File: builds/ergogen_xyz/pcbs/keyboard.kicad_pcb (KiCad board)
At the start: 2 copper layers, 248 x 123.7 mm, 72 parts

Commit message: Phase 2: assembly hardware, wood cutting files, combined 3D render
- Add M2 mounting holes to PCB and outlines (4 corners per half)
- Add frame_with_holes outline for wood CNC/laser cutting
- Generate assembly.scad stacking all layers (frame, plates, PCB)
- Render assembly.png via OpenSCAD
- Update BOM with Phase 1 tenting mount and Phase 2 screws/standoffs
- Update render.md with assembly and wood cutting viewing instructions
- Update generate.sh with assembly generation and OpenSCAD render step

Co-Authored-By: Claude Opus 4.6 <noreply@anthropic.com>
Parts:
- added MH1: , MountingHole_M2, F.Cu at (0.28, -43.3)
- added MH2: , MountingHole_M2, F.Cu at (-5.57, 4.35)
- added MH3: , MountingHole_M2, F.Cu at (90.5, -33.5)
- added MH4: , MountingHole_M2, F.Cu at (80.6, 13.4)
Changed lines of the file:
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@@
         (pad 2 thru_hole circle (at 3.81 0 68) (size 1.905 1.905) (drill 0.9906) (layers *.Cu *.Mask) (net 36 "mirror_far_thumb"))
     )
+      (module MountingHole_M2 (layer F.Cu)
+      (at 0.27765109999999993 -43.2888312 -7)
+      (fp_text reference "MH1" (at 0 -2.5) (layer F.SilkS) hide (effects (font (size 1 1) (thickness 0.15))))
+      (fp_text value "" (at 0 0) (layer F.Fab) hide (effects (font (size 1 1) (thickness 0.15))))
+      (pad "" np_thru_hole circle (at 0 0) (size 2.2 2.2) (drill 2.2) (layers *.Cu *.Mask))
+      (fp_circle (center 0 0) (end 2 0) (layer F.CrtYd) (width 0.05))
+      (fp_circle (center 0 0) (end 2 0) (layer F.SilkS) (width 0.1))
+      )
+      (module MountingHole_M2 (layer F.Cu)
+      (at -5.5720775 4.353384 -7)
+      (fp_text reference "MH2" (at 0 -2.5) (layer F.SilkS) hide (effects (font (size 1 1) (thickness 0.15))))
+      (fp_text value "" (at 0 0) (layer F.Fab) hide (effects (font (size 1 1) (thickness 0.15))))
+      (pad "" np_thru_hole circle (at 0 0) (size 2.2 2.2) (drill 2.2) (layers *.Cu *.Mask))
+      (fp_circle (center 0 0) (end 2 0) (layer F.CrtYd) (width 0.05))
+      (fp_circle (center 0 0) (end 2 0) (layer F.SilkS) (width 0.1))
+      )
+      (module MountingHole_M2 (layer F.Cu)
+      (at 90.5365383 -33.5461871 -12)
+      (fp_text reference "MH3" (at 0 -2.5) (layer F.SilkS) hide (effects (font (size 1 1) (thickness 0.15))))
+      (fp_text value "" (at 0 0) (layer F.Fab) hide (effects (font (size 1 1) (thickness 0.15))))
+      (pad "" np_thru_hole circle (at 0 0) (size 2.2 2.2) (drill 2.2) (layers *.Cu *.Mask))
+      (fp_circle (center 0 0) (end 2 0) (layer F.CrtYd) (width 0.05))
+      (fp_circle (center 0 0) (end 2 0) (layer F.SilkS) (width 0.1))
+      )
+      (module MountingHole_M2 (layer F.Cu)
+      (at 80.556777 13.4048977 -12)
+      (fp_text reference "MH4" (at 0 -2.5) (layer F.SilkS) hide (effects (font (size 1 1) (thickness 0.15))))
+      (fp_text value "" (at 0 0) (layer F.Fab) hide (effects (font (size 1 1) (thickness 0.15))))
+      (pad "" np_thru_hole circle (at 0 0) (size 2.2 2.2) (drill 2.2) (layers *.Cu *.Mask))
+      (fp_circle (center 0 0) (end 2 0) (layer F.CrtYd) (width 0.05))
+      (fp_circle (center 0 0) (end 2 0) (layer F.SilkS) (width 0.1))
+      )
   (gr_line (start -8.044647100170188 8.079829999782175) (end 5.850999096811741 9.786000824362372) (angle 90) (layer Edge.Cuts) (width 0.15))
 (gr_line (start 8.079829999782177 8.044647100170181) (end 8.689176698708792 3.0819165121198893) (angle 90) (layer Edge.Cuts) (width 0.15))

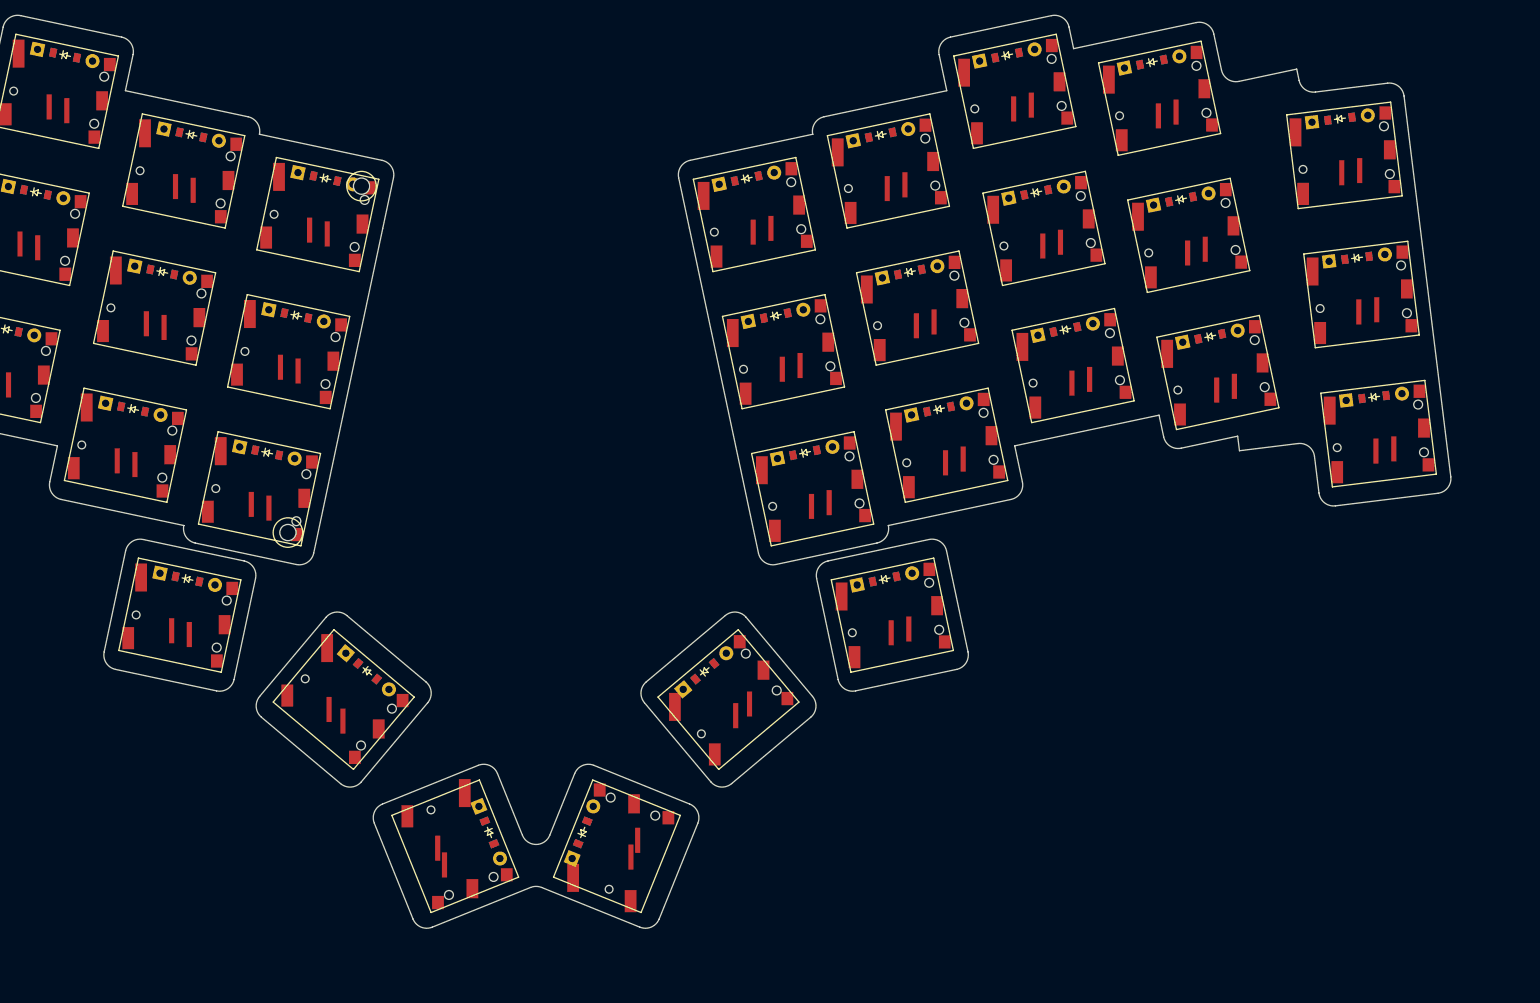
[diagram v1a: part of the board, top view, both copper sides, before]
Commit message: Redesign: cables + hinge folding, thumb support, MCU in 3D, thinner
Design changes per updated requirements:
- Remove tenting mechanism, replace with two horizontal cables
  (top Q-P, bottom Z-M) connecting halves with hook quick-detach
- Add lockable ball bearing hinge at center for folding
- Fix thumb cluster: bridge outlines so frame/plate/PCB cover all
  thumb keys (no more floating keys)
- Add nice!nano MCU + USB-C to 3D assembly model
- Reduce thickness from 7.3mm to 3.8mm by removing standoffs,
  thinning plates (1.0mm bottom, 1.2mm switch plate)
- assembly.scad is now the interactive viewer (openscad with
  rotate/zoom/cross-section), not just static PNG
- Update BOM: replace turnbuckle tenting with cables/hooks/hinge
- Update render.md with interactive viewer instructions

Co-Authored-By: Claude Opus 4.6 <noreply@anthropic.com>
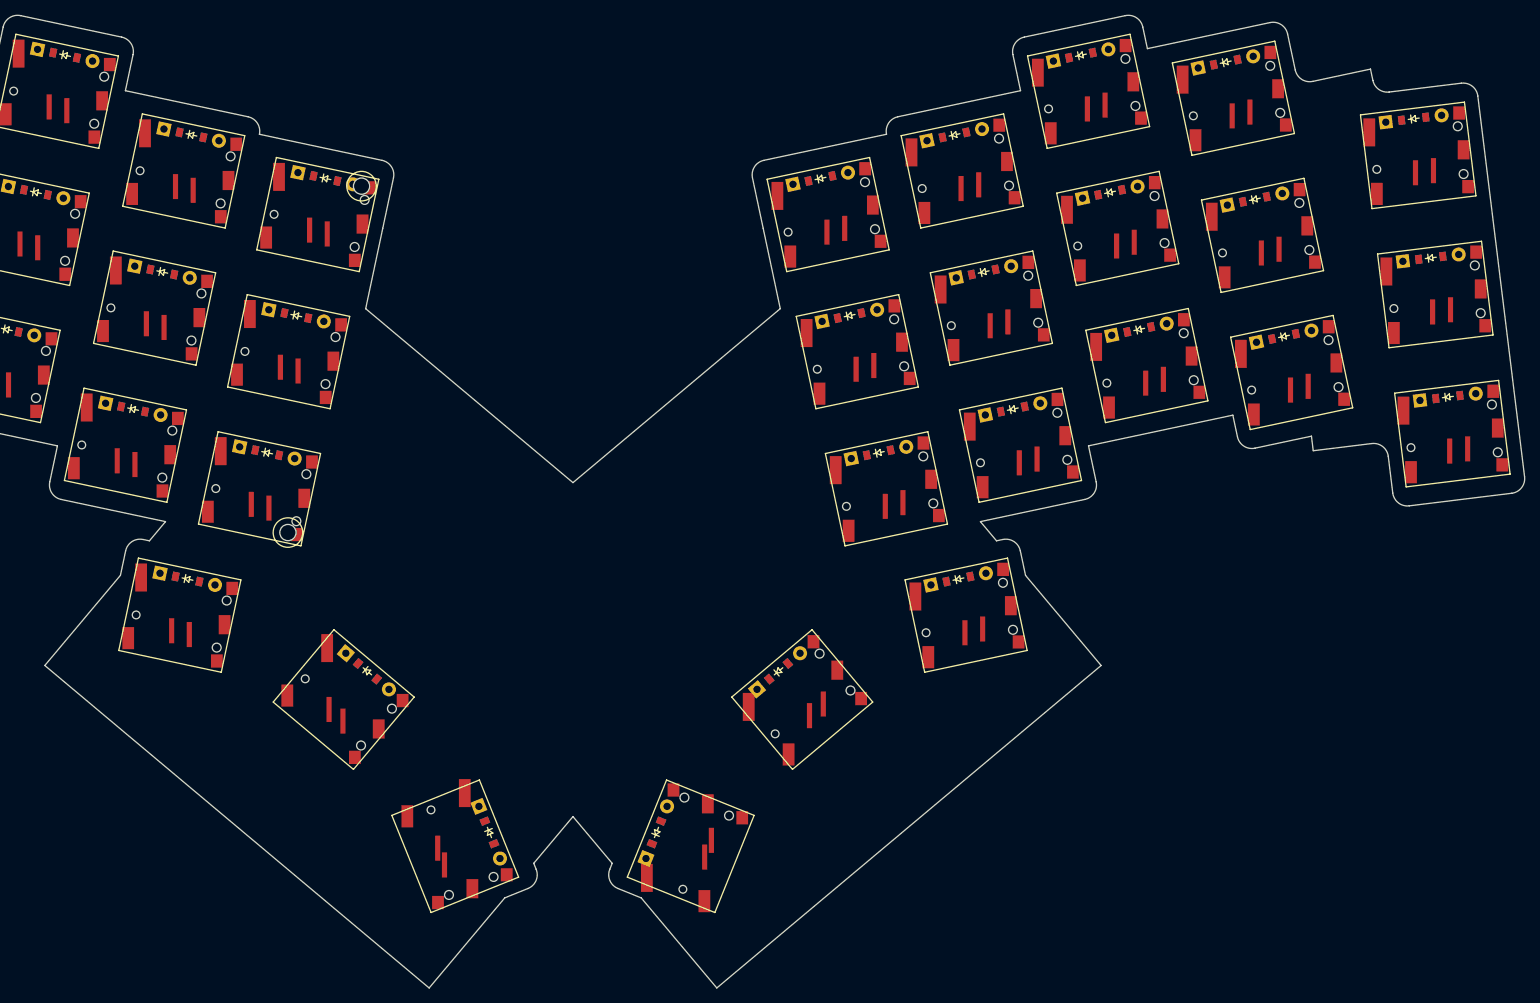
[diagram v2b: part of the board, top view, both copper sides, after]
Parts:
- moved S36 10.0 mm to (135.1, 55.9)
- moved D19 10.0 mm to (237.8, -4.96)
- moved D20 10.0 mm to (235.5, -23.8)
- moved D21 10.0 mm to (233.1, -42.7)
- moved D22 10.0 mm to (215.6, -13.2)
- moved D23 10.0 mm to (211.6, -31.8)
- moved D24 10.0 mm to (207.7, -50.3)
- moved D25 10.0 mm to (195.9, -14.1)
- moved D26 10.0 mm to (192.0, -32.7)
- moved D27 10.0 mm to (188.0, -51.3)
- moved D28 10.0 mm to (178.8, -3.32)
- moved D29 10.0 mm to (174.9, -21.9)
- moved D30 10.0 mm to (170.9, -40.5)
- moved D31 10.0 mm to (160.6, 2.58)
- moved D32 10.0 mm to (156.7, -16.0)
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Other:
- board size 248 x 123.7 mm -> 258 x 131.8 mm
